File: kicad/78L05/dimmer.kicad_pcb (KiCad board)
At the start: 2 copper layers, 25.4 x 35.6 mm, 12 parts, among them IC1 ATTINY85-S, P1 CONN_01X02, P2 CONN_01X02, Q1 Q_NMOS_GDS, SW2 TACTILE_SW, SW4 TACTILE_SW, U1 MC78L05ACH

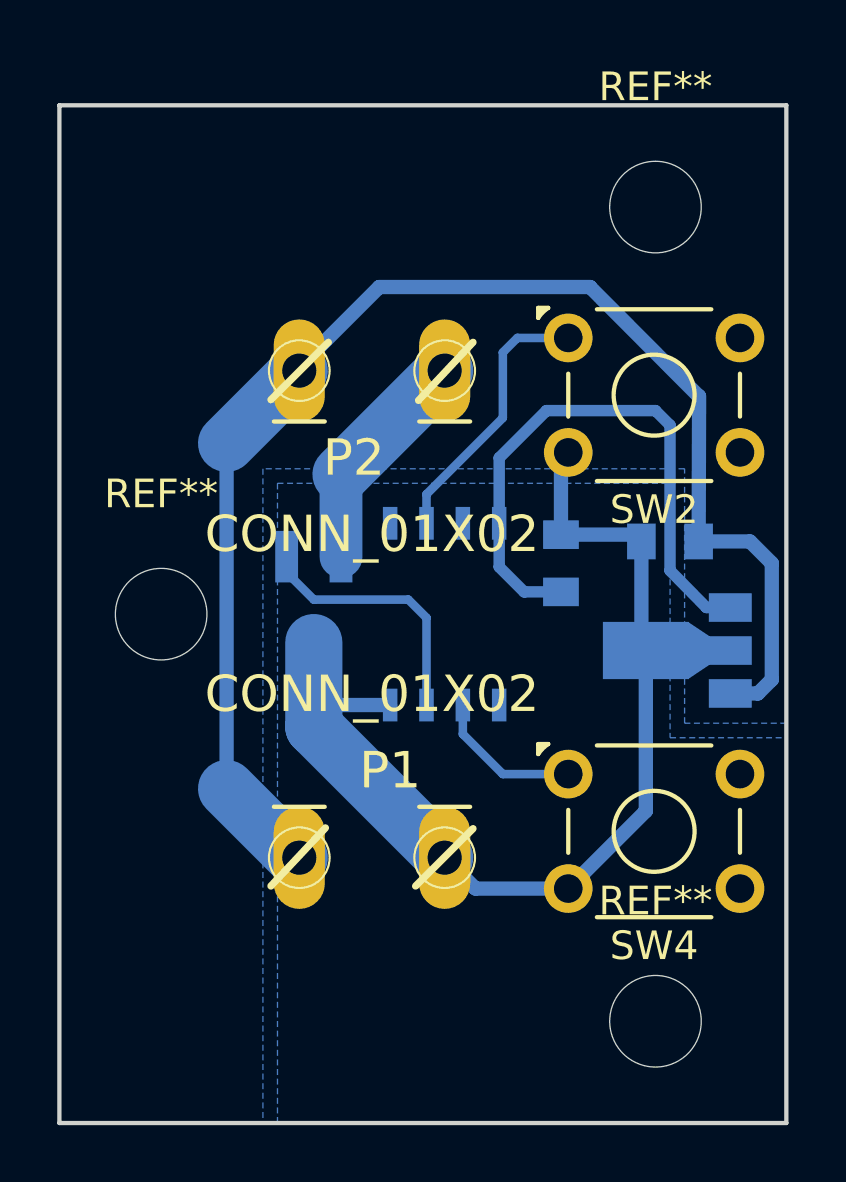
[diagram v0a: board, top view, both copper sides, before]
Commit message: 78L05 PCB: added guard diode
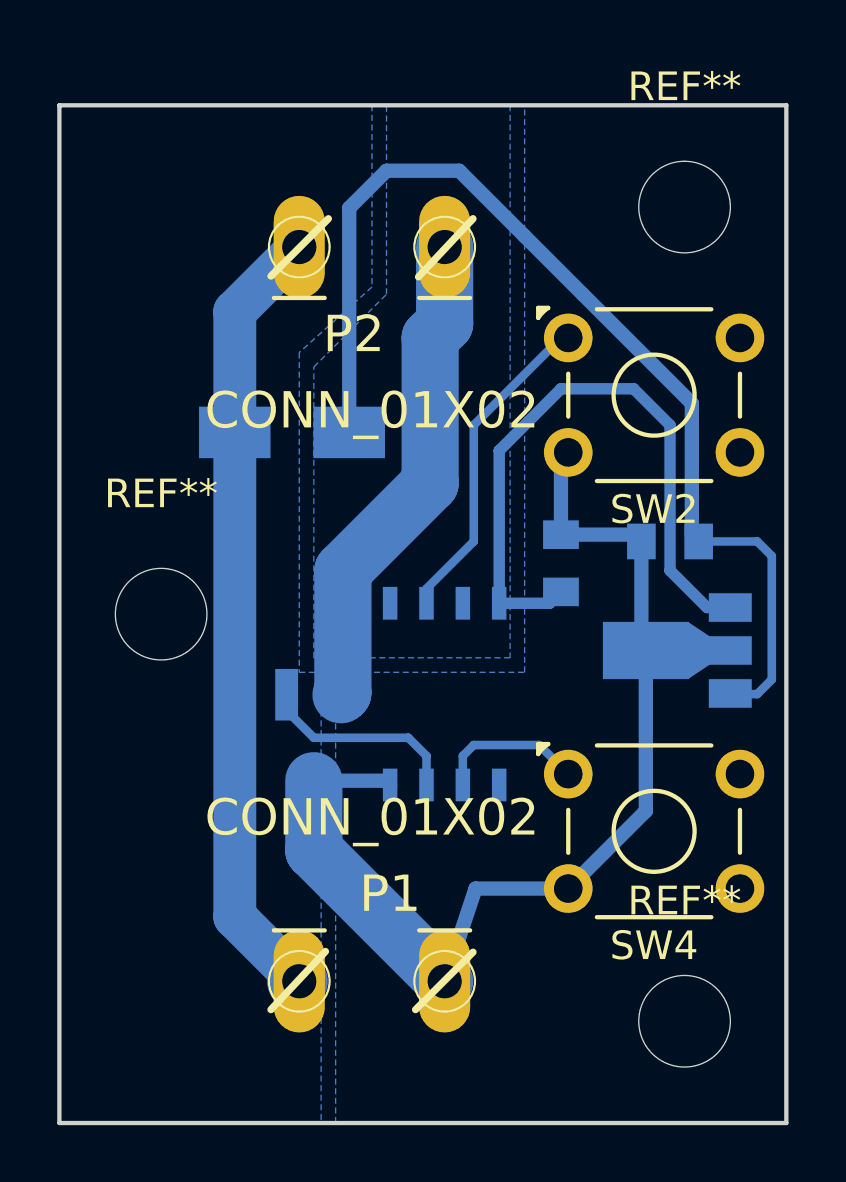
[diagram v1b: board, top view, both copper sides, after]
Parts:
- added D1: D_Small, Diodes_SMD:SMA_Standard, B.Cu at (188.7, 122.7)
- moved Q1 4.83 mm to (189.5, 133.3)
- moved P1 4.32 mm to (191.5, 142.5)
- moved P2 4.32 mm to (191.5, 115.6)
- moved IC1 2.79 mm to (194.1, 131.8)
- moved REF** 1.02 mm to (202.4, 143.3)
- moved REF** 1.02 mm to (202.4, 114.8)
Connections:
- C1 pad 1: +12V -> Net-(C1-Pad1)
- U1 pad 3: +12V -> Net-(C1-Pad1)
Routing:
- net Net-(C1-Pad1): track 0.00 -> 37.4 mm
- net +12V: track 49.7 -> 27.8 mm
- net /out: track 8.00 -> 17.1 mm
- net Net-(IC1-Pad6): track 9.57 -> 11.7 mm
- net Net-(IC1-Pad3): track 9.14 -> 7.11 mm
- net +5V: track 20.9 -> 22.8 mm
- net GND: track 39.8 -> 40.7 mm
- added copper zone on B.Cu, net /out
